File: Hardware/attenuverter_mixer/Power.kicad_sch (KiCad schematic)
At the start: 11 parts, among them J10 euro_power_10, U1 TL074, U2 TL074

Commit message: created fabrication output
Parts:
- C10, C11, C12, C9: LCSC (none) -> C14663
- D1, D2: LCSC (none) -> C82046; MFR Micro Commercial Co -> ONSEMI; MPN MBR0530-TP -> MBR0530T1G
- U1, U2: LCSC (none) -> C96507
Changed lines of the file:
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@@
       (effects (font (size 1.27 1.27)) hide)
     )
-    (property "MFR" "Micro Commercial Co" (at 114.3 100.33 0)
-      (effects (font (size 1.27 1.27)) hide)
-    )
-    (property "MPN" "MBR0530-TP" (at 114.3 100.33 0)
+    (property "MFR" "ONSEMI" (at 114.3 100.33 0)
+      (effects (font (size 1.27 1.27)) hide)
+    )
+    (property "MPN" "MBR0530T1G" (at 114.3 100.33 0)
+      (effects (font (size 1.27 1.27)) hide)
+    )
+    (property "LCSC" "C82046" (at 114.3 100.33 0)
       (effects (font (size 1.27 1.27)) hide)
     )
@@
     )
     (property "MPN" "TL074CPWR" (at 203.2 88.9 0)
+      (effects (font (size 1.27 1.27)) hide)
+    )
+    (property "LCSC" "C96507" (at 203.2 88.9 0)
       (effects (font (size 1.27 1.27)) hide)
     )
@@
       (effects (font (size 1.27 1.27)) hide)
     )
+    (property "LCSC" "C14663" (at 154.94 86.36 0)
+      (effects (font (size 1.27 1.27)) hide)
+    )
     (pin "1")
     (pin "2")
@@
       (effects (font (size 1.27 1.27)) hide)
     )
-    (property "MFR" "Micro Commercial Co" (at 105.41 85.09 0)
-      (effects (font (size 1.27 1.27)) hide)
-    )
-    (property "MPN" "MBR0530-TP" (at 105.41 85.09 0)
+    (property "MFR" "ONSEMI" (at 105.41 85.09 0)
+      (effects (font (size 1.27 1.27)) hide)
+    )
+    (property "MPN" "MBR0530T1G" (at 105.41 85.09 0)
+      (effects (font (size 1.27 1.27)) hide)
+    )
+    (property "LCSC" "C82046" (at 105.41 85.09 0)
       (effects (font (size 1.27 1.27)) hide)
     )
@@
       (effects (font (size 1.27 1.27)) hide)
     )
+    (property "LCSC" "" (at 140.97 96.52 0)
+      (effects (font (size 1.27 1.27)) hide)
+    )
     (pin "1")
     (pin "2")
@@
     )
     (property "MPN" "TL074CPWR" (at 191.77 88.9 0)
+      (effects (font (size 1.27 1.27)) hide)
+    )
+    (property "LCSC" "C96507" (at 191.77 88.9 0)
       (effects (font (size 1.27 1.27)) hide)
     )
@@
       (effects (font (size 1.27 1.27)) hide)
     )
+    (property "LCSC" "" (at 140.97 86.36 0)
+      (effects (font (size 1.27 1.27)) hide)
+    )
     (pin "1")
     (pin "2")
@@
       (effects (font (size 1.27 1.27)) hide)
     )
+    (property "LCSC" "C14663" (at 154.94 96.52 0)
+      (effects (font (size 1.27 1.27)) hide)
+    )
     (pin "1")
     (pin "2")
@@
     )
     (property "MPN" "CC0603KRX7R9BB104" (at 167.64 86.36 0)
+      (effects (font (size 1.27 1.27)) hide)
+    )
+    (property "LCSC" "C14663" (at 167.64 86.36 0)
       (effects (font (size 1.27 1.27)) hide)
     )
@@
       (effects (font (size 1.27 1.27)) hide)
     )
+    (property "LCSC" "C14663" (at 167.64 96.52 0)
+      (effects (font (size 1.27 1.27)) hide)
+    )

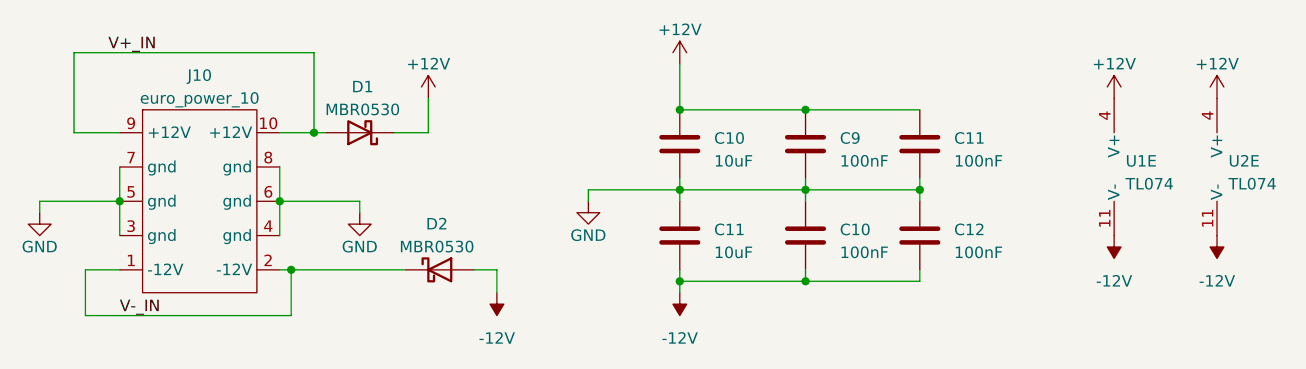
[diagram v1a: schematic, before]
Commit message: proto order
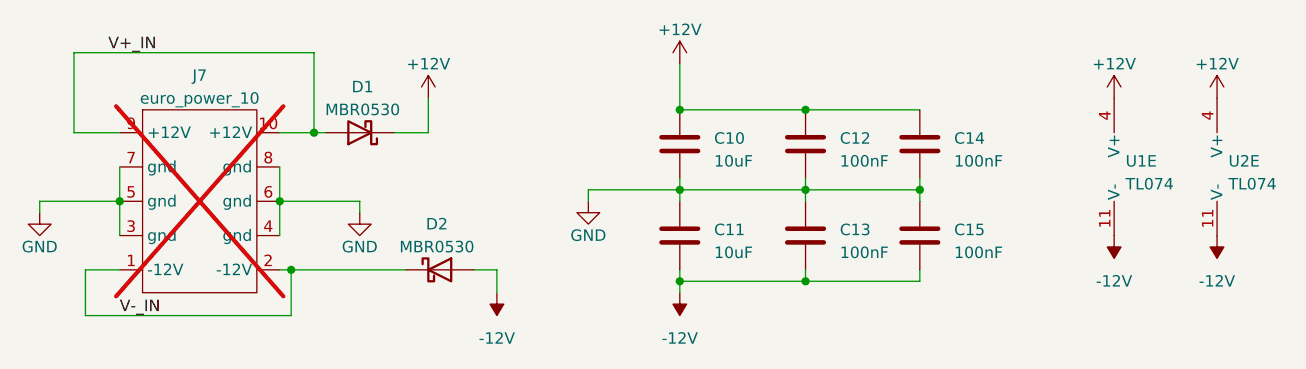
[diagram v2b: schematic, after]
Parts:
- J7: renamed from J10; now not fitted
- renumbered C9 to C12, C10 to C13, C11 to C14, C12 to C15
